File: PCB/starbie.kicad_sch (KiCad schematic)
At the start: 7 parts, among them J1 Conn_01x04_Pin, J2 Conn_01x08_Pin, SW1 SW_Push, SW2 SW_Push, U1 XIAO-ESP32-C3-SMD, U2 DHT11

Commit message: added buzzer to pcb
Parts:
- added BZ1: Buzzer, Connector_PinHeader_2.54mm:PinHeader_1x02_P2.54mm_Vertical, symbol Device:Buzzer
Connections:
- net GND: now also BZ1.2 (-)
- net BUZZER: now reaches U1.7 (D6)
- net BUZZER: now also BZ1.1 (+)
- no-connect marks 17 -> 16
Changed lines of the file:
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@@
-	)
-	(no_connect
-		(at 123.19 102.87)
 	)
 	(no_connect
@@
 	(wire
 		(pts
+			(xy 180.34 99.06) (xy 186.69 99.06)
+		)
+		(stroke
+			(width 0)
+			(type default)
+		)
+	)
+	(wire
+		(pts
+			(xy 113.03 102.87) (xy 123.19 102.87)
+		)
+		(stroke
+			(width 0)
+			(type default)
+		)
+	)
+	(wire
+		(pts
 			(xy 113.03 95.25) (xy 123.19 95.25)
 		)
@@
 	(wire
 		(pts
+			(xy 181.61 105.41) (xy 186.69 105.41)
+		)
+		(stroke
+			(width 0)
+			(type default)
+		)
+	)
+	(wire
+		(pts
 			(xy 138.43 123.19) (xy 138.43 125.73)
 		)
@@
 	(wire
 		(pts
+			(xy 186.69 105.41) (xy 186.69 104.14)
+		)
+		(stroke
+			(width 0)
+			(type default)
+		)
+	)
+	(wire
+		(pts
 			(xy 165.1 80.01) (xy 170.18 80.01)
 		)
@@
 			(width 0)
 			(type default)
+		)
+	)
+	(label "BUZZER"
+		(at 113.03 102.87 0)
+		(effects
+			(font
+				(size 1.27 1.27)
+			)
+			(justify left bottom)
 		)
 	)
@@
 	(label "GPIO3"
 		(at 76.2 82.55 0)
+		(effects
+			(font
+				(size 1.27 1.27)
+			)
+			(justify left bottom)
+		)
+	)
+	(label "BUZZER"
+		(at 180.34 99.06 0)
 		(effects
 			(font
@@
 	)
 	(symbol
+		(lib_id "power:GND")
+		(at 181.61 105.41 0)
+		(unit 1)
+		(body_style 1)
+		(exclude_from_sim no)
+		(in_bom yes)
+		(on_board yes)
+		(in_pos_files yes)
+		(dnp no)
+		(fields_autoplaced yes)
+		(property "Reference" "#PWR014"
+			(at 181.61 111.76 0)
+			(hide yes)
+			(show_name no)
+			(do_not_autoplace no)
+			(effects
+				(font
+					(size 1.27 1.27)
+				)
+			)
+		)
+		(property "Value" "GND"
+			(at 181.61 110.49 0)
+			(show_name no)
+			(do_not_autoplace no)
+			(effects
+				(font
+					(size 1.27 1.27)
+				)
+			)
+		)
+		(property "Footprint" ""
+			(at 181.61 105.41 0)
+			(hide yes)
+			(show_name no)
+			(do_not_autoplace no)
+			(effects
+				(font
+					(size 1.27 1.27)
+				)
+			)
+		)
+		(property "Datasheet" ""
+			(at 181.61 105.41 0)
+			(hide yes)
+			(show_name no)
+			(do_not_autoplace no)
+			(effects
+				(font
+					(size 1.27 1.27)
+				)
+			)
+		)
+		(property "Description" "Power symbol creates a global label with name \"GND\" , ground"
+			(at 181.61 105.41 0)
+			(hide yes)
+			(show_name no)
+			(do_not_autoplace no)
+			(effects
+				(font
+					(size 1.27 1.27)
+				)
+			)
+		)
+		(pin "1"
+		)
+		(instances
+			(project "starbie"
+				(path "/c64ba189-8838-4801-952b-d10581921eee"
+					(reference "#PWR014")
+					(unit 1)
+				)
+			)
+		)
+	)
+	(symbol
 		(lib_id "power:+3.3V")
 		(at 138.43 123.19 0)
@@
 					(unit 1)
 				)
+			)
+		)
+	)
+	(symbol
+		(lib_id "Device:Buzzer")
+		(at 189.23 101.6 0)
+		(unit 1)
+		(body_style 1)
+		(exclude_from_sim no)
+		(in_bom yes)
+		(on_board yes)
+		(in_pos_files yes)
+		(dnp no)
+		(fields_autoplaced yes)
+		(property "Reference" "BZ1"
+			(at 193.04 100.3299 0)
+			(show_name no)
+			(do_not_autoplace no)
+			(effects
+				(font
+					(size 1.27 1.27)
+				)
+				(justify left)
+			)
+		)
+		(property "Value" "Buzzer"
+			(at 193.04 102.8699 0)
+			(show_name no)
+			(do_not_autoplace no)
+			(effects
+				(font
+					(size 1.27 1.27)
+				)
+				(justify left)
+			)
+		)
+		(property "Footprint" "Connector_PinHeader_2.54mm:PinHeader_1x02_P2.54mm_Vertical"
+			(at 188.595 99.06 90)
+			(hide yes)
+			(show_name no)
+			(do_not_autoplace no)
+			(effects
+				(font
+					(size 1.27 1.27)
+				)
+			)
+		)
+		(property "Datasheet" ""
+			(at 188.595 99.06 90)
+			(hide yes)
+			(show_name no)
+			(do_not_autoplace no)
+			(effects
+				(font
+					(size 1.27 1.27)
+				)
+			)
+		)
+		(property "Description" "Buzzer, polarized"
+			(at 189.23 101.6 0)
+			(hide yes)
+			(show_name no)
+			(do_not_autoplace no)
+			(effects
+				(font
+					(size 1.27 1.27)
+				)
+			)
+		)
+		(pin "1"
+		)
+		(pin "2"
+		)
+		(instances
+			(project "starbie"
+				(path "/c64ba189-8838-4801-952b-d10581921eee"
+					(reference "BZ1")
+					(unit 1)
+				)

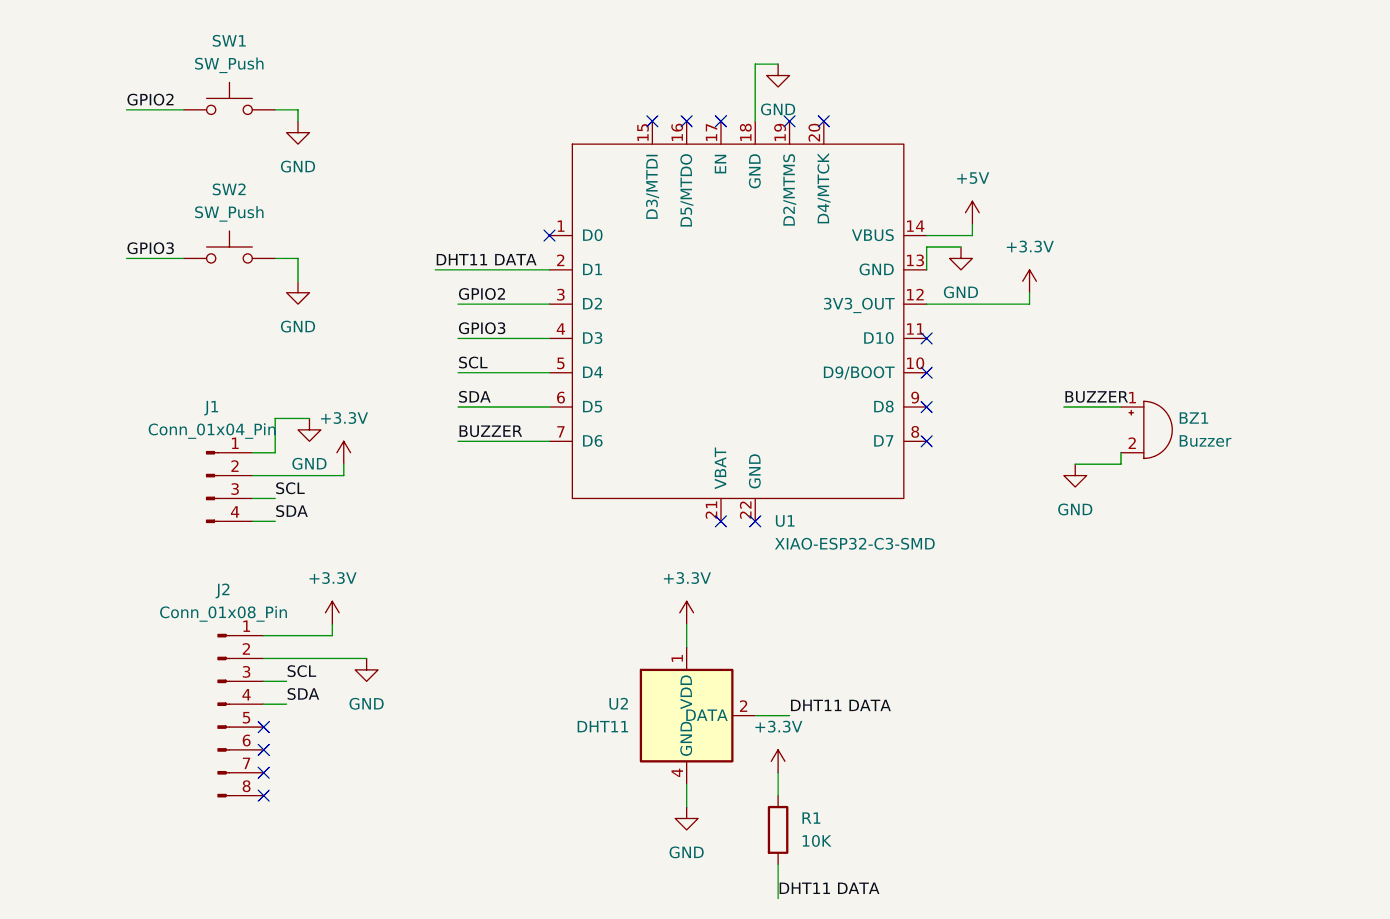
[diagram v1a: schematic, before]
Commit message: realized wrong buzzer, changed pcb routing again
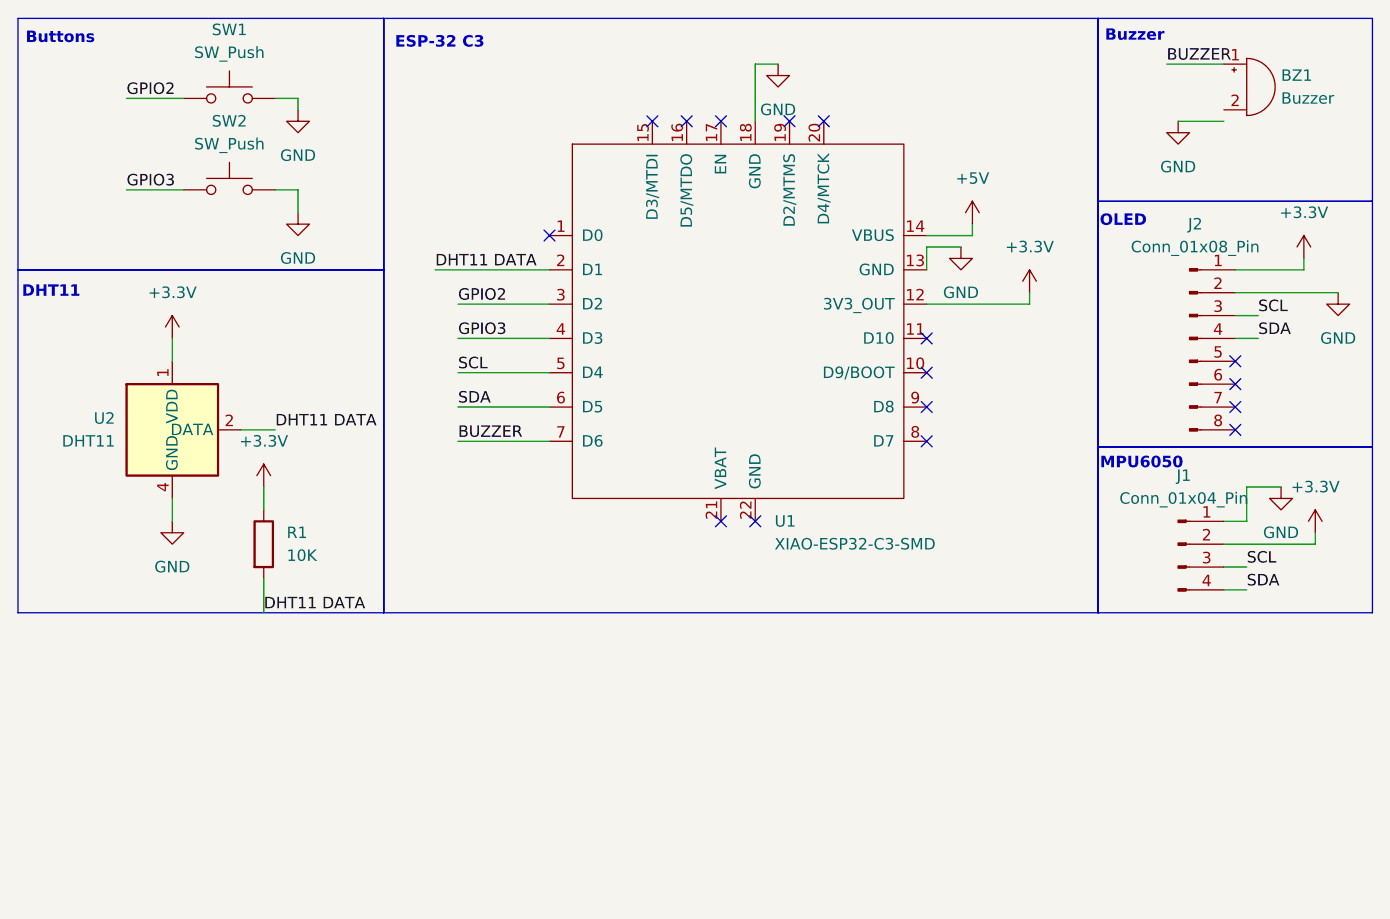
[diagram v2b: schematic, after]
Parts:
- BZ1: footprint Connector_PinHeader_2.54mm:PinHeader_1x02_P2.54mm_Vertical -> Buzzer_Beeper:Buzzer_TDK_PS1240P02BT_D12.2mm_H6.5mm
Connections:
- net GND: no longer BZ1.2 (-)
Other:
- note added: "Buttons"
- note added: "Buzzer"
- note added: "DHT11"
- note added: "ESP-32 C3"
- note added: "MPU6050"
- note added: "OLED"
- moved on the sheet: BZ1, J1, J2, R1, SW1, SW2, U2
